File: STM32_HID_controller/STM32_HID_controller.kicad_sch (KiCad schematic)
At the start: 49 parts, among them J1 USB_B_Micro, J2 Conn_01x04_Pin, J3 Conn_01x03_Pin, J5 Conn_01x03_Pin, SW1 SW_SPDT, SW10 SW_Push, SW11 SW_Push, SW14 SW_Push, SW2 SW_Push, SW3 SW_Push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

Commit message: Started flux for left and right
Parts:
- removed R3: 10k, Resistor_SMD:R_0402_1005Metric, symbol Device:R
- added U6: ADXL343, Package_LGA:LGA-14_3x5mm_P0.8mm_LayoutBorder1x6y, symbol Sensor_Motion:ADXL343
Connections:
- net +: now also U1.57 (PB5); no longer U1.61 (PB8)
- net +3.3V: now also U6.1 (Vdd_I/O), U6.6 (Vs)
- net -: now also U1.61 (PB8); no longer U1.62 (PB9)
- net A: now also U1.25 (PC5); no longer U1.55 (PB3)
- net ACC_control: now also U1.8 (PC0); no longer U1.36 (PB15)
- net B: now also U1.23 (PA7); no longer U1.56 (PB4)
- net GND: now also U6.2 (GND), U6.4 (GND), U6.5 (GND)
- net SCL: now also U1.34 (PB13), U6.14 (SCL/SCLK); no longer U1.29 (PB10)
- net SDI: now also U6.13 (SDA/SDI/SDIO)
- net SDO: now also U6.12 (SDO/ADDR)
- net X: now also U1.26 (PB0); no longer U1.57 (PB5)
- net Y: now also U1.24 (PC4); no longer U1.58 (PB6)
- net capture: now also U1.62 (PB9); no longer U1.38 (PC7)
- net cs: now also U1.11 (PC3), U6.7 (~{CS}); no longer U1.22 (PA6)
- net home: now also U1.56 (PB4); no longer U1.37 (PC6)
- net jl: now also U1.55 (PB3); no longer U1.42 (PA9)
- net jr: now also U1.22 (PA6); no longer U1.41 (PA8)
- net l: now also U1.51 (PC10); no longer U1.35 (PB14)
- net r: now also U1.27 (PB1); no longer U1.43 (PA10)
- net zl: now also U1.52 (PC11); no longer U1.40 (PC9)
- net zr: now also U1.28 (PB2); no longer U1.39 (PC8)
- no-connect marks 29 -> 33

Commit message: final draft
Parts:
- added H7, H8: MountingHole, MountingHole:MountingHole_2.2mm_M2, symbol Mechanical:MountingHole
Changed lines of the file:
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@@
 	(symbol
 		(lib_id "Mechanical:MountingHole")
+		(at 74.93 71.12 0)
+		(unit 1)
+		(exclude_from_sim no)
+		(in_bom no)
+		(on_board yes)
+		(dnp no)
+		(fields_autoplaced yes)
+		(property "Reference" "H7"
+			(at 77.47 69.8499 0)
+			(effects
+				(font
+					(size 1.27 1.27)
+				)
+				(justify left)
+			)
+		)
+		(property "Value" "MountingHole"
+			(at 77.47 72.3899 0)
+			(effects
+				(font
+					(size 1.27 1.27)
+				)
+				(justify left)
+			)
+		)
+		(property "Footprint" "MountingHole:MountingHole_2.2mm_M2"
+			(at 74.93 71.12 0)
+			(effects
+				(font
+					(size 1.27 1.27)
+				)
+				(hide yes)
+			)
+		)
+		(property "Datasheet" "~"
+			(at 74.93 71.12 0)
+			(effects
+				(font
+					(size 1.27 1.27)
+				)
+				(hide yes)
+			)
+		)
+		(property "Description" "Mounting Hole without connection"
+			(at 74.93 71.12 0)
+			(effects
+				(font
+					(size 1.27 1.27)
+				)
+				(hide yes)
+			)
+		)
+		(instances
+			(project ""
+				(path "/93f508db-e88d-474d-97a3-a9b92fae4357"
+					(reference "H7")
+					(unit 1)
+				)
+			)
+		)
+	)
+	(symbol
+		(lib_id "Mechanical:MountingHole")
 		(at 77.47 21.59 0)
 		(unit 1)
@@
 					(unit 1)
 				)
+			)
+		)
+	)
+	(symbol
+		(lib_id "Mechanical:MountingHole")
+		(at 74.93 77.47 0)
+		(unit 1)
+		(exclude_from_sim no)
+		(in_bom no)
+		(on_board yes)
+		(dnp no)
+		(fields_autoplaced yes)
+		(property "Reference" "H8"
+			(at 77.47 76.1999 0)
+			(effects
+				(font
+					(size 1.27 1.27)
+				)
+				(justify left)
+			)
+		)
+		(property "Value" "MountingHole"
+			(at 77.47 78.7399 0)
+			(effects
+				(font
+					(size 1.27 1.27)
+				)
+				(justify left)
+			)
+		)
+		(property "Footprint" "MountingHole:MountingHole_2.2mm_M2"
+			(at 74.93 77.47 0)
+			(effects
+				(font
+					(size 1.27 1.27)
+				)
+				(hide yes)
+			)
+		)
+		(property "Datasheet" "~"
+			(at 74.93 77.47 0)
+			(effects
+				(font
+					(size 1.27 1.27)
+				)
+				(hide yes)
+			)
+		)
+		(property "Description" "Mounting Hole without connection"
+			(at 74.93 77.47 0)
+			(effects
+				(font
+					(size 1.27 1.27)
+				)
+				(hide yes)
+			)
+		)
+		(instances
+			(project "STM32_HID_controller"
+				(path "/93f508db-e88d-474d-97a3-a9b92fae4357"
+					(reference "H8")
+					(unit 1)
+				)

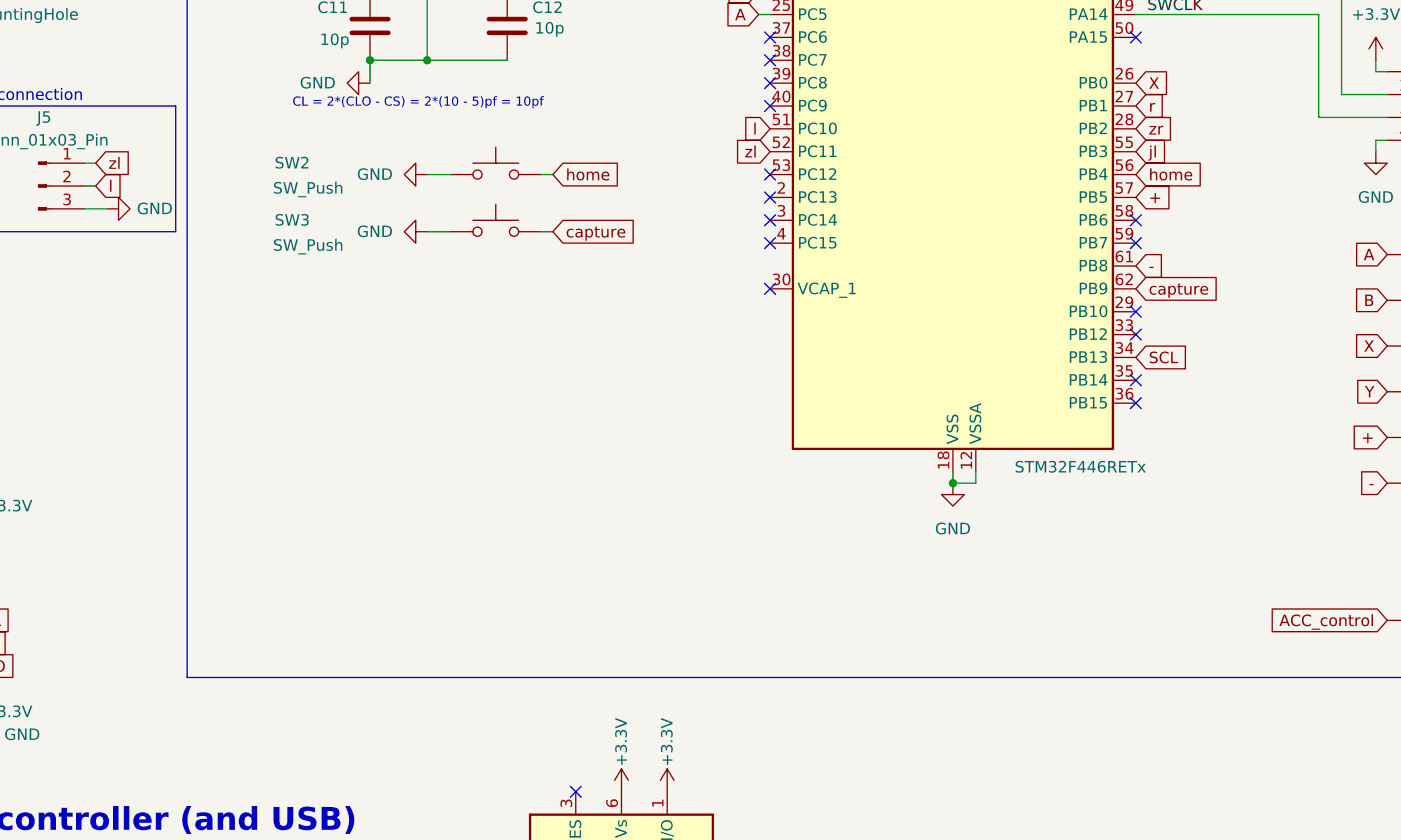
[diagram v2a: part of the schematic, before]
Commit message: added mpu
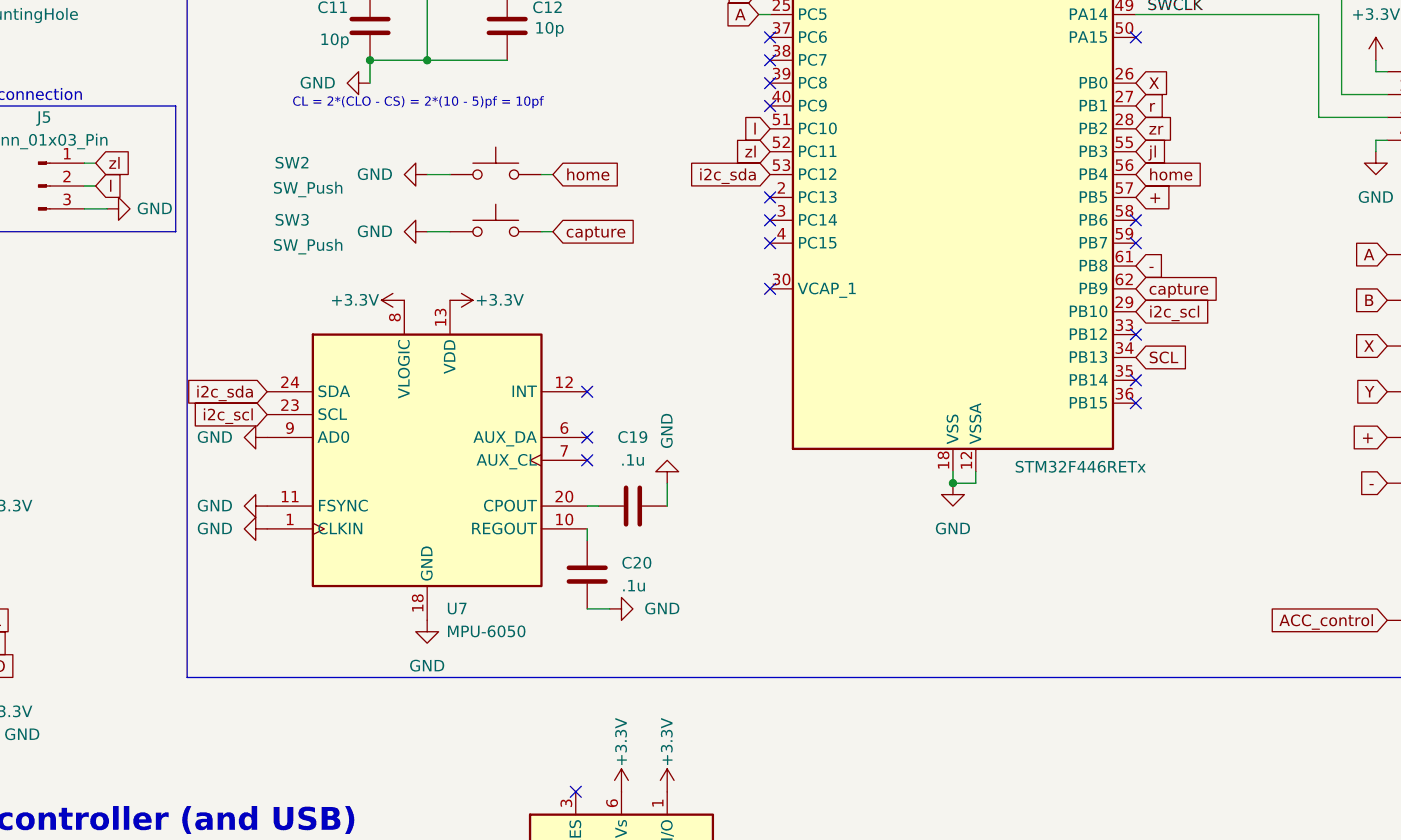
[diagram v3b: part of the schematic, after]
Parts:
- added C19, C20: .1u, Capacitor_SMD:C_0402_1005Metric, symbol Device:C
- added U7: MPU-6050, Sensor_Motion:InvenSense_QFN-24_4x4mm_P0.5mm, symbol Sensor_Motion:MPU-6050
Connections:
- net +3.3V: now also U7.13 (VDD), U7.8 (VLOGIC)
- net GND: now also C19.2, C20.2, U7.1 (CLKIN), U7.11 (FSYNC), U7.18 (GND), U7.9 (AD0)
- net i2c_scl: now reaches U1.29 (PB10)
- net i2c_scl: now also U7.23 (SCL)
- net i2c_sda: now reaches U1.53 (PC12)
- net i2c_sda: now also U7.24 (SDA)
- new net: C19.1, U7.20 (CPOUT)
- new net: C20.1, U7.10 (REGOUT)
- no-connect marks 33 -> 34

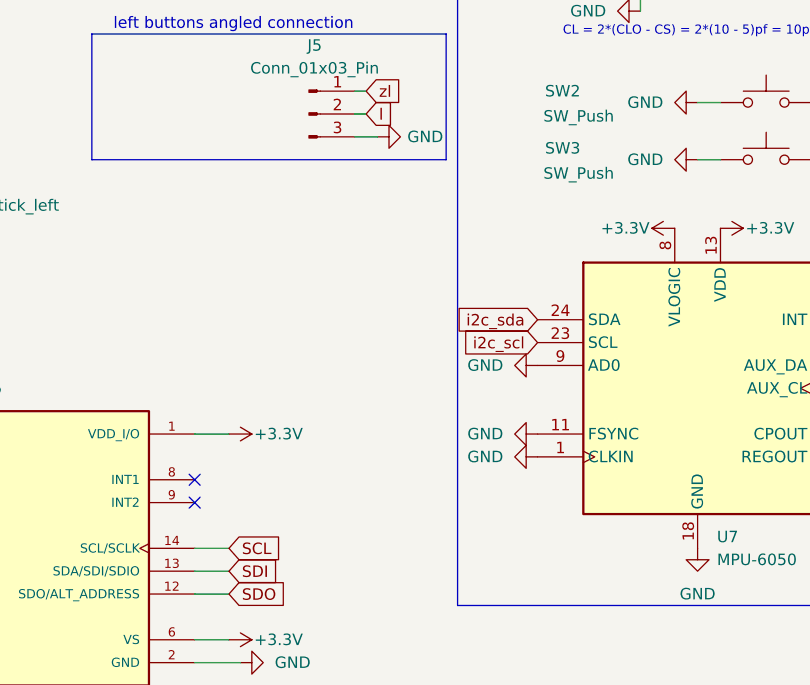
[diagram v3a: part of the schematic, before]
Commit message: mpu6050 pull ups
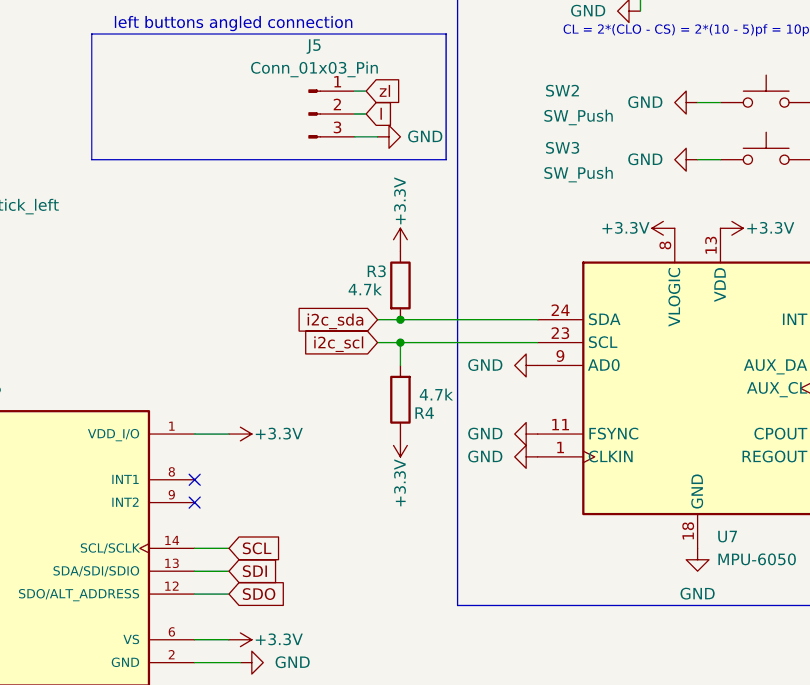
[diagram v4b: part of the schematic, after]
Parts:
- added R3, R4: 4.7k, symbol Device:R
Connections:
- net +3.3V: now also R3.1, R4.1
- net i2c_scl: now also R4.2
- net i2c_sda: now also R3.2

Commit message: added mpu to everything, final draft before review
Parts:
- R3, R4: footprint (none) -> Resistor_SMD:R_0402_1005Metric
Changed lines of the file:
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@@
 			)
 		)
-		(property "Footprint" ""
+		(property "Footprint" "Resistor_SMD:R_0402_1005Metric"
 			(at 93.472 116.84 90)
 			(effects
@@
 			)
 		)
-		(property "Footprint" ""
+		(property "Footprint" "Resistor_SMD:R_0402_1005Metric"
 			(at 97.028 129.54 90)
 			(effects
